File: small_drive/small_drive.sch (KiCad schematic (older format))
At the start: 159 parts, among them J1 DB9, J2 DB15, M1 SiR826DP, M2 SiR826DP, M3 SiR826DP, M4 SiR826DP, M5 SiR826DP, M6 SiR826DP, P1 CONN_01X04, P2 CONN_01X04, P3 CONN_01X04, P4 CONN_01X04, P5 CONN_01X02, P6 CONN_01X02, P7 CONN_01X02, P8 CONN_01X01, U1 XMC4400-F64x512, U10 LM5106, U11 ACS711KLCTR-12AB-T, U12 ACS711ELCTR-25AB-T, U13 ACS711KLCTR-12AB-T, U14 AD8226, U15 MAX3096, U16 AMC1203, U17 7805, U18 LT1764EQ, U19 KSZ8081, U2 ips511g, U20 ETH100_MAG, U3 ips511g, U4 LTC2850, U5 AD8226, U6 LT1764EQ, U7 MC33074DTBR2, U8 LM5106, U9 LM5106, X1 NKE1212DC, X2 NKE1212DC, X3 HCPL0201, X4 HCPL0201, X5 HCPL0201, X6 HCPL0201, Y1 12MHz, Y2 25MHz

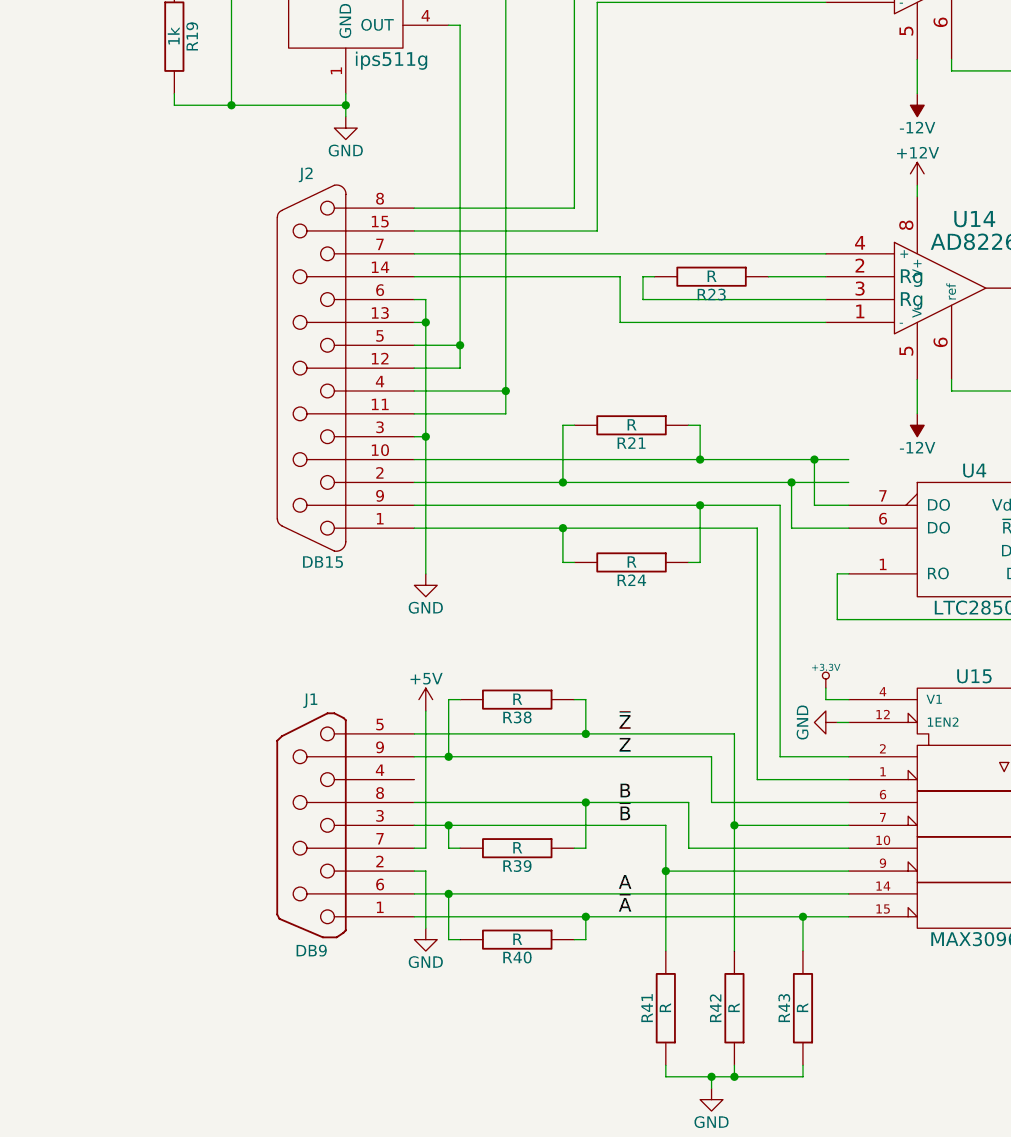
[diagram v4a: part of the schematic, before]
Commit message: Functional PWM, including subsampling interrupt.
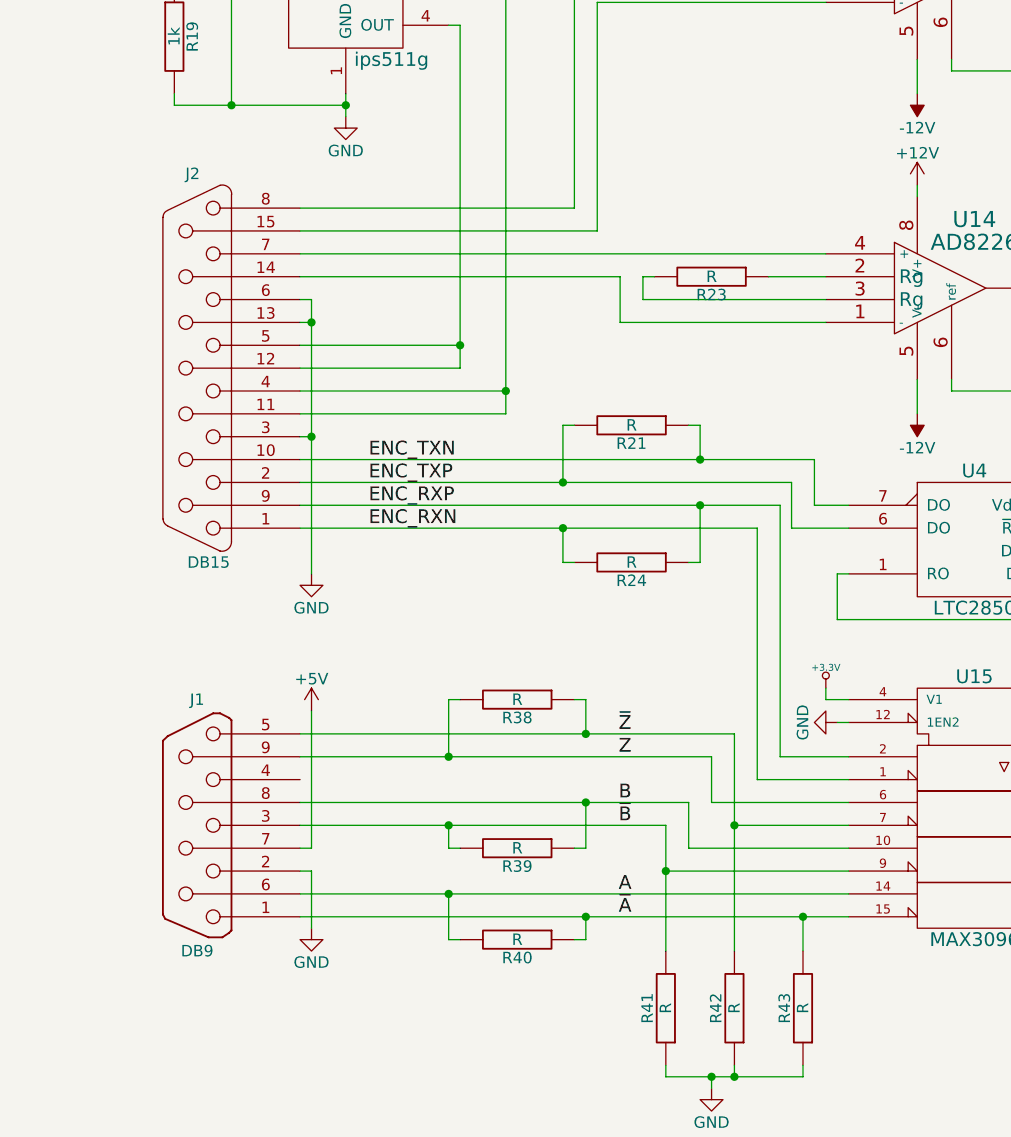
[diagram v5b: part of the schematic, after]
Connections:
- net labels added: ENC_RXN, ENC_RXP, ENC_TXN, ENC_TXP
- wire segments 901 -> 899
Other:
- moved on the sheet: J1, J2
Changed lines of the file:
@@
 L DB9 J1
 U 1 1 57797C40
-P 9850 14000
-F 0 "J1" H 9850 14550 50  0000 C CNN
-F 1 "DB9" H 9850 13450 50  0000 C CNN
-F 2 "Connectors_Amphenol:DB9FC_HD-20" H 9850 14000 50  0001 C CNN
-F 3 "" H 9850 14000 50  0000 C CNN
-F 4 "1653978" H 9850 14000 60  0001 C CNN "Farnell"
-F 5 "AMP" H 9850 14000 60  0001 C CNN "Manufacturer"
-F 6 "1734354-1" H 9850 14000 60  0001 C CNN "PartNr"
-	1    9850 14000
+P 9350 14000
+F 0 "J1" H 9350 14550 50  0000 C CNN
+F 1 "DB9" H 9350 13450 50  0000 C CNN
+F 2 "Connectors_Amphenol:DB9FC_HD-20" H 9350 14000 50  0001 C CNN
+F 3 "" H 9350 14000 50  0000 C CNN
+F 4 "1653978" H 9350 14000 60  0001 C CNN "Farnell"
+F 5 "AMP" H 9350 14000 60  0001 C CNN "Manufacturer"
+F 6 "1734354-1" H 9350 14000 60  0001 C CNN "PartNr"
+	1    9350 14000
 	-1   0    0    -1
 $EndComp
@@
 L +5V #PWR08
 U 1 1 57798829
-P 10350 13500
-F 0 "#PWR08" H 10350 13350 50  0001 C CNN
-F 1 "+5V" H 10350 13640 50  0000 C CNN
-F 2 "" H 10350 13500 50  0000 C CNN
-F 3 "" H 10350 13500 50  0000 C CNN
-	1    10350 13500
+P 9850 13500
+F 0 "#PWR08" H 9850 13350 50  0001 C CNN
+F 1 "+5V" H 9850 13640 50  0000 C CNN
+F 2 "" H 9850 13500 50  0000 C CNN
+F 3 "" H 9850 13500 50  0000 C CNN
+	1    9850 13500
 	-1   0    0    -1
 $EndComp
@@
 L GND-RESCUE-small_drive #PWR09
 U 1 1 57798BD2
-P 10350 14450
-F 0 "#PWR09" H 10350 14200 50  0001 C CNN
-F 1 "GND" H 10350 14300 50  0000 C CNN
-F 2 "" H 10350 14450 50  0000 C CNN
-F 3 "" H 10350 14450 50  0000 C CNN
-	1    10350 14450
+P 9850 14450
+F 0 "#PWR09" H 9850 14200 50  0001 C CNN
+F 1 "GND" H 9850 14300 50  0000 C CNN
+F 2 "" H 9850 14450 50  0000 C CNN
+F 3 "" H 9850 14450 50  0000 C CNN
+	1    9850 14450
 	-1   0    0    -1
 $EndComp
@@
 L DB15 J2
 U 1 1 57A78B2E
-P 9850 12000
-F 0 "J2" H 9870 12850 50  0000 C CNN
-F 1 "DB15" H 9800 11150 50  0000 C CNN
-F 2 "Connectors_Amphenol:DB15F_HD20_SIZE2" H 9850 12000 50  0001 C CNN
-F 3 "" H 9850 12000 50  0000 C CNN
-F 4 "3417207" H 9850 12000 60  0001 C CNN "Farnell"
-F 5 "AMP" H 9850 12000 60  0001 C CNN "Manufacturer"
-F 6 "1-106506-2" H 9850 12000 60  0001 C CNN "PartNr"
-	1    9850 12000
+P 9350 12000
+F 0 "J2" H 9370 12850 50  0000 C CNN
+F 1 "DB15" H 9300 11150 50  0000 C CNN
+F 2 "Connectors_Amphenol:DB15F_HD20_SIZE2" H 9350 12000 50  0001 C CNN
+F 3 "" H 9350 12000 50  0000 C CNN
+F 4 "3417207" H 9350 12000 60  0001 C CNN "Farnell"
+F 5 "AMP" H 9350 12000 60  0001 C CNN "Manufacturer"
+F 6 "1-106506-2" H 9350 12000 60  0001 C CNN "PartNr"
+	1    9350 12000
 	-1   0    0    -1
 $EndComp
@@
 L GND #PWR031
 U 1 1 57AA32DE
-P 10350 12900
-F 0 "#PWR031" H 10350 12650 50  0001 C CNN
-F 1 "GND" H 10350 12750 50  0000 C CNN
-F 2 "" H 10350 12900 50  0000 C CNN
-F 3 "" H 10350 12900 50  0000 C CNN
-	1    10350 12900
+P 9850 12900
+F 0 "#PWR031" H 9850 12650 50  0001 C CNN
+F 1 "GND" H 9850 12750 50  0000 C CNN
+F 2 "" H 9850 12900 50  0000 C CNN
+F 3 "" H 9850 12900 50  0000 C CNN
+	1    9850 12900
 	1    0    0    -1
 $EndComp
@@
 	20250 11350 20300 11350
 Wire Wire Line
-	10300 13600 11050 13600
+	9800 13600 11050 13600
 Wire Wire Line
 	11050 13600 11700 13600
 Wire Wire Line
-	10300 13700 10450 13700
+	9800 13700 10450 13700
 Wire Wire Line
 	10450 13700 11600 13700
 Wire Wire Line
-	10300 14300 10450 14300
+	9800 14300 10450 14300
 Wire Wire Line
 	10450 14300 12200 14300
 Wire Wire Line
-	10300 14400 11050 14400
+	9800 14400 11050 14400
 Wire Wire Line
 	11050 14400 12000 14400
@@
 	12000 14400 12200 14400
 Wire Wire Line
-	10350 13500 10350 14100
+	9850 13500 9850 14100
 Wire Wire Line
-	10350 14100 10300 14100
+	9850 14100 9800 14100
 Wire Wire Line
-	10350 14450 10350 14200
+	9850 14450 9850 14200
 Wire Wire Line
-	10350 14200 10300 14200
+	9850 14200 9800 14200
 Wire Wire Line
 	2950 9300 2950 9400
@@
 Connection ~ 10100 1100
 Wire Wire Line
-	10300 13900 11050 13900
+	9800 13900 11050 13900
 Wire Wire Line
 	11050 13900 11500 13900
 Wire Wire Line
-	10300 14000 10450 14000
+	9800 14000 10450 14000
 Wire Wire Line
 	10450 14000 11400 14000
@@
 	13300 14350 13900 14350
 Wire Wire Line
-	10300 12400 11550 12400
+	9800 12400 11550 12400
 Wire Wire Line
 	11550 12400 12050 12400
 Wire Wire Line
-	12050 12400 12200 12400
-Wire Wire Line
-	10300 12500 10950 12500
+	9800 12500 10950 12500
 Wire Wire Line
 	10950 12500 11950 12500
 Wire Wire Line
-	11950 12500 12200 12500
-Wire Wire Line
 	13400 12250 13400 12600
 Wire Wire Line
@@
 	11100 10400 11100 11400
 Wire Wire Line
-	11100 11400 10300 11400
+	11100 11400 9800 11400
 Wire Wire Line
-	10300 11300 11000 11300
+	9800 11300 11000 11300
 Wire Wire Line
 	11000 11300 11000 10100
@@
 	12100 11800 11200 11800
 Wire Wire Line
-	10300 11500 12100 11500
+	9800 11500 12100 11500
 Wire Wire Line
 	12500 11200 12500 11250
@@
 	11200 11800 11200 11600
 Wire Wire Line
-	11200 11600 10300 11600
+	11200 11600 9800 11600
 Wire Wire Line
 	11300 11700 11300 11600
@@
 	10450 9300 10700 9300
 Wire Wire Line
-	10300 11700 10350 11700
+	9800 11700 9850 11700
 Wire Wire Line
-	10350 11700 10350 11800
+	9850 11700 9850 11800
 Wire Wire Line
-	10350 11800 10350 12300
+	9850 11800 9850 12300
 Wire Wire Line
-	10350 12300 10350 12900
+	9850 12300 9850 12900
 Wire Wire Line
-	10350 11800 10300 11800
+	9850 11800 9800 11800
 Wire Wire Line
-	10300 11900 10500 11900
+	9800 11900 10500 11900
 Wire Wire Line
-	10500 12000 10300 12000
+	10500 12000 9800 12000
 Wire Wire Line
 	10500 10500 10500 11900
@@
 Connection ~ 10500 11900
 Wire Wire Line
-	10350 12300 10300 12300
-Connection ~ 10350 11800
-Connection ~ 10350 12300
+	9850 12300 9800 12300
+Connection ~ 9850 11800
+Connection ~ 9850 12300
 Wire Wire Line
-	10700 12200 10300 12200
+	10700 12200 9800 12200
 Wire Wire Line
 	10700 9300 10700 12100
@@
 	10700 12100 10700 12200
 Wire Wire Line
-	10300 12100 10700 12100
+	9800 12100 10700 12100
 Connection ~ 10700 12100
 Wire Wire Line
@@
 Wire Wire Line
 	11950 12700 12200 12700
-Connection ~ 11950 12500
 Wire Wire Line
 	12050 12400 12050 12600
 Wire Wire Line
 	12050 12600 12200 12600
-Connection ~ 12050 12400
 Wire Wire Line
 	11500 12250 11550 12250
@@
 Connection ~ 10950 12500
 Wire Wire Line
-	10300 12700 10950 12700
+	9800 12700 10950 12700
 Wire Wire Line
 	10950 12700 11800 12700
@@
 	11800 12700 11800 13800
 Wire Wire Line
-	10300 12600 11550 12600
+	9800 12600 11550 12600
 Wire Wire Line
 	11550 12600 11900 12600
@@
 Text Notes 4950 14000 0    60   ~ 0
 MAX3096 package too big.\nUpdate ethernet jack\nAdd pullup to ETH0_MDIO
+Text Label 10100 12400 0    60   ~ 0
+ENC_TXN
+Text Label 10100 12500 0    60   ~ 0
+ENC_TXP
+Text Label 10100 12600 0    60   ~ 0
+ENC_RXP
+Text Label 10100 12700 0    60   ~ 0
+ENC_RXN
 $EndSCHEMATC

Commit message: Working logger on board.
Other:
- note added: "MAX3096 package too big.\nUpdate ethernet jack\nAdd pullup to ETH0_MDIO\nENC_Z and ENC_RXD2 swapped"
- note removed: "MAX3096 package too big.\nUpdate ethernet jack\nAdd pullup to ETH0_MDIO"
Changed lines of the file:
@@
 Text Label 2050 7650 0    60   ~ 0
 ETH0_RXERA
-Text Label 2100 7550 0    60   ~ 0
+Text Label 2050 7550 0    60   ~ 0
 ETH0_TX_EN
 Text Label 2100 11650 0    60   ~ 0
@@
 SWCLK
 Text Notes 4950 14000 0    60   ~ 0
-MAX3096 package too big.\nUpdate ethernet jack\nAdd pullup to ETH0_MDIO
+MAX3096 package too big.\nUpdate ethernet jack\nAdd pullup to ETH0_MDIO\nENC_Z and ENC_RXD2 swapped
 Text Label 10100 12400 0    60   ~ 0
 ENC_TXN

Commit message: Allow different encoders.
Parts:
- U20: Farnell (none) -> 2676003
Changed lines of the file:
@@
 F 2 "00_Passives:ETH100_MAG" H 10600 7300 60  0001 C CNN
 F 3 "SI-50170-F.pdf" H 10600 6950 60  0001 C CNN
-F 4 "SI-50170-F" H 11000 8375 60  0001 C CNN "PartNr"
+F 4 "2676003" H 10600 6900 60  0001 C CNN "Farnell"
 F 5 "380-1103-ND" H 10600 6750 60  0001 C CNN "Digikey"
 F 6 "Bel_Stewart" H 10600 6850 60  0001 C CNN "Manufacturer"
+F 7 "SI-50170-F" H 11000 8375 60  0001 C CNN "PartNr"
 	1    10600 6900
 	1    0    0    -1

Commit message: DSD works for the AMC1204.
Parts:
- R22, R23: value R -> 4.7k
- R25, R26: value 1k -> 510
- R27, R28: value 510 -> 1k
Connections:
- wire segments 899 -> 666
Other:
- note added: "MAX3096 package too big.\nUpdate ethernet jack\nAdd pullup to ETH0_MDIO\nENC_Z and ENC_RXD2 swapped\nMake ENC_TXD bi-directional (to be tested)\nMove sincos ADC channels to G2 an G3 (to be tested)\nMCLK and MDAT swapped"
- note removed: "MAX3096 package too big.\nUpdate ethernet jack\nAdd pullup to ETH0_MDIO\nENC_Z and ENC_RXD2 swapped"
